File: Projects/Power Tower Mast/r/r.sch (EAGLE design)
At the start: 29 parts

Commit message: updated with extra vias and panelized
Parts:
- added VIN1, VO10, VO11, VO12, VO13, VO14, VO8, VO9: (no value), CyberRailGuru:TEST_POINTPAD1-20
- renumbered TP1 to VO1, TP2 to VO2, TP3 to VO3, TP4 to VO4, TP5 to VO5, TP6 to VO6, TP7 to VO7, TP8 to VIN
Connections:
- removed net VIN5: LED1.A, LED10.A, LED13.A, LED16.A, LED19.A, LED4.A, LED7.A, VIN.TP
- removed net VOUT26: LED3.C, VO1.TP
- removed net VOUT27: LED6.C, VO2.TP
- removed net VOUT28: LED9.C, VO3.TP
- removed net VOUT29: LED12.C, VO4.TP
- removed net VOUT30: LED15.C, VO5.TP
- removed net VOUT31: LED18.C, VO6.TP
- removed net VOUT32: LED21.C, VO7.TP
- new net VIN: LED1.A, LED10.A, LED13.A, LED16.A, LED19.A, LED4.A, LED7.A, VIN.TP, VIN1.TP
- new net VOUT1: LED3.C, VO1.TP, VO8.TP
- new net VOUT2: LED6.C, VO2.TP, VO9.TP
- new net VOUT3: LED9.C, VO10.TP, VO3.TP
- new net VOUT4: LED12.C, VO11.TP, VO4.TP
- new net VOUT5: LED15.C, VO12.TP, VO5.TP
- new net VOUT6: LED18.C, VO13.TP, VO6.TP
- new net VOUT7: LED21.C, VO14.TP, VO7.TP

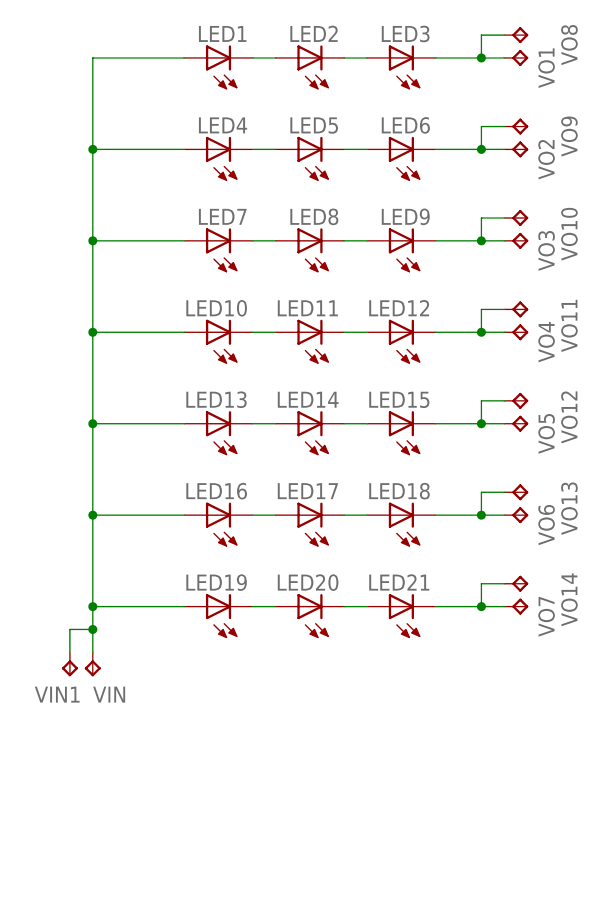
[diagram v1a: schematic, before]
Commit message: fixed ratio for all letters; continued to update layouts
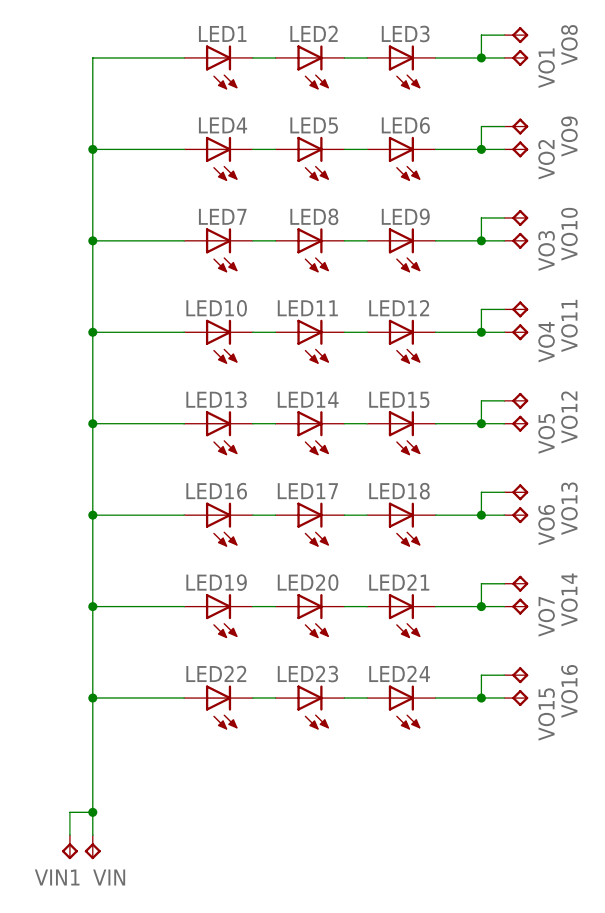
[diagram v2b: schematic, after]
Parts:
- added LED22, LED23, LED24: (no value), CyberRailGuru:LED0805
- added VO15, VO16: (no value), CyberRailGuru:TEST_POINTPAD1-20
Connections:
- new net N$1: LED23.C, LED24.A
- new net N$2: LED22.C, LED23.A
- new net N$3: LED24.C, VO15.TP, VO16.TP
- net VIN: now also LED22.A
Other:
- moved on the sheet: VIN, VIN1
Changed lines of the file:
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@@
 <part name="VO13" library="CyberRailGuru" deviceset="TEST_POINT" device="PAD1-20"/>
 <part name="VO14" library="CyberRailGuru" deviceset="TEST_POINT" device="PAD1-20"/>
+<part name="LED22" library="CyberRailGuru" deviceset="LED" device="0805"/>
+<part name="LED23" library="CyberRailGuru" deviceset="LED" device="0805"/>
+<part name="LED24" library="CyberRailGuru" deviceset="LED" device="0805"/>
+<part name="VO15" library="CyberRailGuru" deviceset="TEST_POINT" device="PAD1-20"/>
+<part name="VO16" library="CyberRailGuru" deviceset="TEST_POINT" device="PAD1-20"/>
 </parts>
 <sheets>
@@
 <instance part="LED20" gate="G$1" x="73.66" y="144.78" rot="R90"/>
 <instance part="LED19" gate="G$1" x="63.5" y="144.78" rot="R90"/>
-<instance part="VIN" gate="G$1" x="50.8" y="137.16" smashed="yes" rot="R180">
-<attribute name="NAME" x="54.61" y="135.89" size="1.778" layer="95" rot="R180"/>
-<attribute name="VALUE" x="49.53" y="138.43" size="1.778" layer="96" rot="R180"/>
+<instance part="VIN" gate="G$1" x="50.8" y="116.84" smashed="yes" rot="R180">
+<attribute name="NAME" x="54.61" y="115.57" size="1.778" layer="95" rot="R180"/>
+<attribute name="VALUE" x="49.53" y="118.11" size="1.778" layer="96" rot="R180"/>
 </instance>
 <instance part="VO1" gate="G$1" x="99.06" y="205.74" smashed="yes" rot="R270">
@@
 <attribute name="VALUE" x="97.79" y="143.51" size="1.778" layer="96" rot="R270"/>
 </instance>
-<instance part="VIN1" gate="G$1" x="48.26" y="137.16" smashed="yes" rot="R180">
-<attribute name="NAME" x="49.53" y="135.89" size="1.778" layer="95" rot="R180"/>
-<attribute name="VALUE" x="46.99" y="138.43" size="1.778" layer="96" rot="R180"/>
+<instance part="VIN1" gate="G$1" x="48.26" y="116.84" smashed="yes" rot="R180">
+<attribute name="NAME" x="49.53" y="115.57" size="1.778" layer="95" rot="R180"/>
+<attribute name="VALUE" x="46.99" y="118.11" size="1.778" layer="96" rot="R180"/>
 </instance>
 <instance part="VO8" gate="G$1" x="99.06" y="208.28" smashed="yes" rot="R270">
@@
 <attribute name="NAME" x="102.87" y="148.59" size="1.778" layer="95" rot="R270"/>
 <attribute name="VALUE" x="97.79" y="146.05" size="1.778" layer="96" rot="R270"/>
+</instance>
+<instance part="LED22" gate="G$1" x="63.5" y="134.62" rot="R90"/>
+<instance part="LED23" gate="G$1" x="73.66" y="134.62" rot="R90"/>
+<instance part="LED24" gate="G$1" x="83.82" y="134.62" rot="R90"/>
+<instance part="VO15" gate="G$1" x="99.06" y="134.62" smashed="yes" rot="R270">
+<attribute name="NAME" x="100.33" y="135.89" size="1.778" layer="95" rot="R270"/>
+<attribute name="VALUE" x="97.79" y="133.35" size="1.778" layer="96" rot="R270"/>
+</instance>
+<instance part="VO16" gate="G$1" x="99.06" y="137.16" smashed="yes" rot="R270">
+<attribute name="NAME" x="102.87" y="138.43" size="1.778" layer="95" rot="R270"/>
+<attribute name="VALUE" x="97.79" y="135.89" size="1.778" layer="96" rot="R270"/>
 </instance>
 </instances>
@@
 <wire x1="50.8" y1="165.1" x2="50.8" y2="154.94" width="0.1524" layer="91"/>
 <wire x1="50.8" y1="154.94" x2="50.8" y2="144.78" width="0.1524" layer="91"/>
-<wire x1="50.8" y1="144.78" x2="50.8" y2="142.24" width="0.1524" layer="91"/>
-<wire x1="50.8" y1="142.24" x2="50.8" y2="139.7" width="0.1524" layer="91"/>
+<wire x1="50.8" y1="144.78" x2="50.8" y2="134.62" width="0.1524" layer="91"/>
+<wire x1="50.8" y1="134.62" x2="50.8" y2="121.92" width="0.1524" layer="91"/>
+<wire x1="50.8" y1="121.92" x2="50.8" y2="119.38" width="0.1524" layer="91"/>
 <wire x1="60.96" y1="144.78" x2="50.8" y2="144.78" width="0.1524" layer="91"/>
 <pinref part="LED16" gate="G$1" pin="A"/>
@@
 <pinref part="VIN" gate="G$1" pin="TP"/>
 <pinref part="VIN1" gate="G$1" pin="TP"/>
-<wire x1="50.8" y1="142.24" x2="48.26" y2="142.24" width="0.1524" layer="91"/>
-<wire x1="48.26" y1="142.24" x2="48.26" y2="139.7" width="0.1524" layer="91"/>
-<junction x="50.8" y="142.24"/>
-</segment>
-</net>
+<wire x1="50.8" y1="121.92" x2="48.26" y2="121.92" width="0.1524" layer="91"/>
+<wire x1="48.26" y1="121.92" x2="48.26" y2="119.38" width="0.1524" layer="91"/>
+<junction x="50.8" y="121.92"/>
+<pinref part="LED22" gate="G$1" pin="A"/>
+<wire x1="60.96" y1="134.62" x2="50.8" y2="134.62" width="0.1524" layer="91"/>
+<junction x="50.8" y="134.62"/>
+</segment>
+</net>
+<net name="N$1" class="0">
+<segment>
+<pinref part="LED23" gate="G$1" pin="C"/>
+<pinref part="LED24" gate="G$1" pin="A"/>
+<wire x1="81.28" y1="134.62" x2="78.74" y2="134.62" width="0.1524" layer="91"/>
+</segment>
+</net>
+<net name="N$2" class="0">
+<segment>
+<pinref part="LED23" gate="G$1" pin="A"/>
+<pinref part="LED22" gate="G$1" pin="C"/>
+<wire x1="68.58" y1="134.62" x2="71.12" y2="134.62" width="0.1524" layer="91"/>
+</segment>
+</net>
+<net name="N$3" class="0">
+<segment>
+<pinref part="LED24" gate="G$1" pin="C"/>
+<pinref part="VO15" gate="G$1" pin="TP"/>
+<wire x1="88.9" y1="134.62" x2="93.98" y2="134.62" width="0.1524" layer="91"/>
+<pinref part="VO16" gate="G$1" pin="TP"/>
+<wire x1="93.98" y1="134.62" x2="96.52" y2="134.62" width="0.1524" layer="91"/>
+<wire x1="96.52" y1="137.16" x2="93.98" y2="137.16" width="0.1524" layer="91"/>
+<wire x1="93.98" y1="137.16" x2="93.98" y2="134.62" width="0.1524" layer="91"/>
+<junction x="93.98" y="134.62"/>
+</segment>
+</net>
